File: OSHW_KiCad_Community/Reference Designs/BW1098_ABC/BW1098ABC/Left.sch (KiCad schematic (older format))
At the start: 20 parts, among them J2 BBR43-24KB533 for camera modu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

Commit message: got abc deriv reference started. Pulled in connectors etc
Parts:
- removed C10, C12, C8: 10uF 0603, symbol depthAI_sch:GRM188R61A106ME69D
- removed C11, C7, C9: 0.1uF 0402, symbol depthAI_sch:GRM188R61A106ME69D
- removed FB4, FB5, FB6: 600R/100MHz, symbol depthAI_sch:2508056017Y2
- removed J2: BBR43-24KB533 for camera module TG161B-201, symbol depthAI_sch:TG161B-201_Connector
- removed R10, R4, R5, R6, R7, R8, R9: 0R 0603, symbol depthAI_sch:CRCW06030000Z0EA
- removed R11, R3: 10K 0402, symbol depthAI_sch:RC0402FR-1310KL
- removed R12: 0R 0402, symbol depthAI_sch:CRCW04020000Z0ED
- added C? (x3): 10uF 0603, symbol depthAI_sch:GRM188R61A106ME69D
- added C? (x3): 0.1uF 0402, symbol depthAI_sch:GRM188R61A106ME69D
- added FB? (x3): 600R/100MHz, symbol depthAI_sch:2508056017Y2
- added J?: BBR43-24KB533 for camera module TG161B-201, symbol depthAI_sch:TG161B-201_Connector
- added R? (x7): 0R 0603, symbol depthAI_sch:CRCW06030000Z0EA
- added R? (x2): 10K 0402, symbol depthAI_sch:RC0402FR-1310KL
- added R?: 0R 0402, symbol depthAI_sch:CRCW04020000Z0ED
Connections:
- net labels removed: 10V
- wire segments 87 -> 84

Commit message: skeleton complete, most footprints assigned, still need to check the transferred ones for dims
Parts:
- C? (x3): footprint (none) -> Capacitor_SMD:C_0201_0603Metric
- C? (x3): footprint (none) -> Capacitor_SMD:C_01005_0402Metric
- FB? (x3): footprint (none) -> Ferrite_THT:LairdTech_28C0236-0JW-10
- R? (x10): footprint (none) -> Resistor_SMD:R_0402_1005Metric
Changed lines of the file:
@@
 $Descr A3 16535 11693
 encoding utf-8
-Sheet 5 5
+Sheet 5 6
 Title ""
 Date ""
@@
 F 0 "FB?" H 1400 950 60  0000 L BNN
 F 1 "600R/100MHz" H 1400 770 60  0000 L BNN
-F 2 "" H 1400 770 60  0001 C CNN
+F 2 "Ferrite_THT:LairdTech_28C0236-0JW-10" H 1400 770 60  0001 C CNN
 F 3 "" H 1400 770 60  0000 C CNN
 	1    1300 900
@@
 F 0 "C?" V 6810 5760 60  0000 R TNN
 F 1 "10uF 0603" V 6710 5760 60  0000 R TNN
-F 2 "" H 6710 5760 60  0001 C CNN
+F 2 "Capacitor_SMD:C_0201_0603Metric" H 6710 5760 60  0001 C CNN
 F 3 "" H 6710 5760 60  0000 C CNN
 F 4 "10V" V 700 750 60  0001 C CNN "Voltage Rating"
@@
 F 0 "C?" V 6210 5760 60  0000 R TNN
 F 1 "0.1uF 0402" V 6110 5760 60  0000 R TNN
-F 2 "" H 6110 5760 60  0001 C CNN
+F 2 "Capacitor_SMD:C_01005_0402Metric" H 6110 5760 60  0001 C CNN
 F 3 "" H 6110 5760 60  0000 C CNN
 F 4 "10V" V 700 750 60  0001 C CNN "Voltage Rating"
@@
 F 0 "C?" V 7510 5760 60  0000 R TNN
 F 1 "0.1uF 0402" V 7410 5760 60  0000 R TNN
-F 2 "" H 7410 5760 60  0001 C CNN
+F 2 "Capacitor_SMD:C_01005_0402Metric" H 7410 5760 60  0001 C CNN
 F 3 "" H 7410 5760 60  0000 C CNN
 F 4 "10V" V 700 750 60  0001 C CNN "Voltage Rating"
@@
 F 0 "R?" V 2910 6320 60  0000 R TNN
 F 1 "0R 0603" V 2810 6320 60  0000 R TNN
-F 2 "" H 2810 6320 60  0001 C CNN
+F 2 "Resistor_SMD:R_0402_1005Metric" H 2810 6320 60  0001 C CNN
 F 3 "" H 2810 6320 60  0000 C CNN
 	1    2700 6350
@@
 F 0 "R?" V 3410 6320 60  0000 R TNN
 F 1 "0R 0603" V 3310 6320 60  0000 R TNN
-F 2 "" H 3310 6320 60  0001 C CNN
+F 2 "Resistor_SMD:R_0402_1005Metric" H 3310 6320 60  0001 C CNN
 F 3 "" H 3310 6320 60  0000 C CNN
 	1    3200 6350
@@
 F 0 "R?" V 3910 6320 60  0000 R TNN
 F 1 "0R 0603" V 3810 6320 60  0000 R TNN
-F 2 "" H 3810 6320 60  0001 C CNN
+F 2 "Resistor_SMD:R_0402_1005Metric" H 3810 6320 60  0001 C CNN
 F 3 "" H 3810 6320 60  0000 C CNN
 	1    3700 6350
@@
 F 0 "R?" H 3340 5930 60  0000 L BNN
 F 1 "0R 0603" H 3340 5770 60  0000 L BNN
-F 2 "" H 3340 5770 60  0001 C CNN
+F 2 "Resistor_SMD:R_0402_1005Metric" H 3340 5770 60  0001 C CNN
 F 3 "" H 3340 5770 60  0000 C CNN
 	1    3250 5900
@@
 F 0 "R?" H 2840 5930 60  0000 L BNN
 F 1 "0R 0603" H 2840 5770 60  0000 L BNN
-F 2 "" H 2840 5770 60  0001 C CNN
+F 2 "Resistor_SMD:R_0402_1005Metric" H 2840 5770 60  0001 C CNN
 F 3 "" H 2840 5770 60  0000 C CNN
 	1    2750 5900
@@
 F 0 "R?" H 3340 6430 60  0000 L BNN
 F 1 "0R 0603" H 3340 6270 60  0000 L BNN
-F 2 "" H 3340 6270 60  0001 C CNN
+F 2 "Resistor_SMD:R_0402_1005Metric" H 3340 6270 60  0001 C CNN
 F 3 "" H 3340 6270 60  0000 C CNN
 	1    3250 6400
@@
 F 0 "FB?" H 1400 1250 60  0000 L BNN
 F 1 "600R/100MHz" H 1400 1070 60  0000 L BNN
-F 2 "" H 1400 1070 60  0001 C CNN
+F 2 "Ferrite_THT:LairdTech_28C0236-0JW-10" H 1400 1070 60  0001 C CNN
 F 3 "" H 1400 1070 60  0000 C CNN
 	1    1300 1200
@@
 F 0 "R?" H 2840 6430 60  0000 L BNN
 F 1 "0R 0603" H 2840 6270 60  0000 L BNN
-F 2 "" H 2840 6270 60  0001 C CNN
+F 2 "Resistor_SMD:R_0402_1005Metric" H 2840 6270 60  0001 C CNN
 F 3 "" H 2840 6270 60  0000 C CNN
 	1    2750 6400
@@
 F 0 "FB?" H 1400 1550 60  0000 L BNN
 F 1 "600R/100MHz" H 1400 1370 60  0000 L BNN
-F 2 "" H 1400 1370 60  0001 C CNN
+F 2 "Ferrite_THT:LairdTech_28C0236-0JW-10" H 1400 1370 60  0001 C CNN
 F 3 "" H 1400 1370 60  0000 C CNN
 	1    1300 1500
@@
 F 0 "R?" H 2290 6880 60  0000 L BNN
 F 1 "10K 0402" H 2290 6720 60  0000 L BNN
-F 2 "" H 2290 6720 60  0001 C CNN
+F 2 "Resistor_SMD:R_0402_1005Metric" H 2290 6720 60  0001 C CNN
 F 3 "" H 2290 6720 60  0000 C CNN
 	1    2200 6850
@@
 F 0 "R?" H 9940 3530 60  0000 L BNN
 F 1 "10K 0402" H 9950 3600 60  0000 L BNN
-F 2 "" H 9940 3370 60  0001 C CNN
+F 2 "Resistor_SMD:R_0402_1005Metric" H 9940 3370 60  0001 C CNN
 F 3 "" H 9940 3370 60  0000 C CNN
 	1    9850 3500
@@
 F 0 "R?" H 9940 3930 60  0000 L BNN
 F 1 "0R 0402" H 9940 3770 60  0000 L BNN
-F 2 "" H 9940 3770 60  0001 C CNN
+F 2 "Resistor_SMD:R_0402_1005Metric" H 9940 3770 60  0001 C CNN
 F 3 "" H 9940 3770 60  0000 C CNN
 	1    9850 3900
@@
 F 0 "C?" V 8710 5760 60  0000 R TNN
 F 1 "0.1uF 0402" V 8610 5760 60  0000 R TNN
-F 2 "" H 8610 5760 60  0001 C CNN
+F 2 "Capacitor_SMD:C_01005_0402Metric" H 8610 5760 60  0001 C CNN
 F 3 "" H 8610 5760 60  0000 C CNN
 F 4 "10V" V 700 750 60  0001 C CNN "Voltage Rating"
@@
 F 0 "C?" V 9310 5760 60  0000 R TNN
 F 1 "10uF 0603" V 9210 5760 60  0000 R TNN
-F 2 "" H 9210 5760 60  0001 C CNN
+F 2 "Capacitor_SMD:C_0201_0603Metric" H 9210 5760 60  0001 C CNN
 F 3 "" H 9210 5760 60  0000 C CNN
 F 4 "10V" V 700 750 60  0001 C CNN "Voltage Rating"
@@
 F 0 "C?" V 8100 5750 60  0000 R TNN
 F 1 "10uF 0603" V 8010 5760 60  0000 R TNN
-F 2 "" H 8010 5760 60  0001 C CNN
+F 2 "Capacitor_SMD:C_0201_0603Metric" H 8010 5760 60  0001 C CNN
 F 3 "" H 8010 5760 60  0000 C CNN
 F 4 "10V" V 700 750 60  0001 C CNN "Voltage Rating"

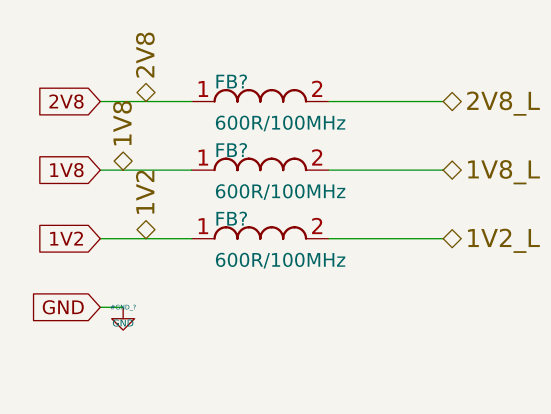
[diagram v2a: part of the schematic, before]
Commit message: schematic edits for BW1098ABC
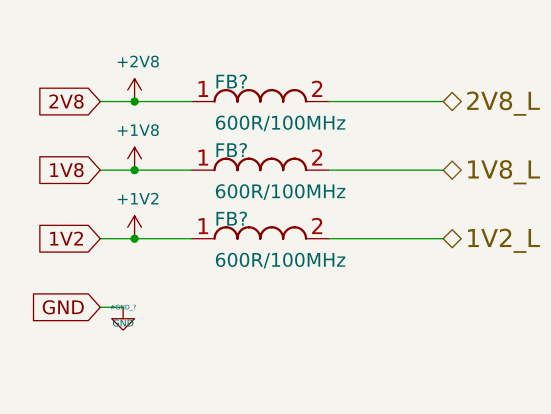
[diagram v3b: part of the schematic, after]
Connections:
- net labels added: +1V2, +1V8, +2V8
- wire segments 84 -> 87
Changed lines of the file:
@@
 $EndBitmap
 Wire Wire Line
-	900  900  1300 900
+	900  900  1050 900
 Wire Wire Line
-	900  1200 1300 1200
-Wire Wire Line
-	900  1500 1300 1500
-Text HLabel 1100 900  1    79   BiDi ~ 0
-2V8
-Text HLabel 1000 1200 1    79   BiDi ~ 0
-1V8
-Text HLabel 1100 1500 1    79   BiDi ~ 0
-1V2
+	900  1500 1050 1500
 Text HLabel 2400 900  2    79   BiDi ~ 0
 2V8_L
@@
 Wire Wire Line
 	8550 3700 10150 3700
+$Comp
+L power:+1V2 #PWR?
+U 1 1 5FFF8485
+P 1050 1500
+AR Path="/604AEAFA/5FFF8485" Ref="#PWR?"  Part="1"
+AR Path="/5FF8D2B3/5FFF8485" Ref="#PWR?"  Part="1"
+F 0 "#PWR?" H 1050 1350 50  0001 C CNN
+F 1 "+1V2" H 1065 1673 50  0000 C CNN
+F 2 "" H 1050 1500 50  0001 C CNN
+F 3 "" H 1050 1500 50  0001 C CNN
+	1    1050 1500
+	1    0    0    -1
+$EndComp
+$Comp
+L power:+1V8 #PWR?
+U 1 1 5FFF848B
+P 1050 1200
+AR Path="/604AEAFA/5FFF848B" Ref="#PWR?"  Part="1"
+AR Path="/5FF8D2B3/5FFF848B" Ref="#PWR?"  Part="1"
+F 0 "#PWR?" H 1050 1050 50  0001 C CNN
+F 1 "+1V8" H 1065 1373 50  0000 C CNN
+F 2 "" H 1050 1200 50  0001 C CNN
+F 3 "" H 1050 1200 50  0001 C CNN
+	1    1050 1200
+	1    0    0    -1
+$EndComp
+$Comp
+L power:+2V8 #PWR?
+U 1 1 5FFF8491
+P 1050 900
+AR Path="/604AEAFA/5FFF8491" Ref="#PWR?"  Part="1"
+AR Path="/5FF8D2B3/5FFF8491" Ref="#PWR?"  Part="1"
+F 0 "#PWR?" H 1050 750 50  0001 C CNN
+F 1 "+2V8" H 1065 1073 50  0000 C CNN
+F 2 "" H 1050 900 50  0001 C CNN
+F 3 "" H 1050 900 50  0001 C CNN
+	1    1050 900
+	1    0    0    -1
+$EndComp
+Connection ~ 1050 900
+Wire Wire Line
+	1050 900  1300 900
+Connection ~ 1050 1200
+Wire Wire Line
+	1050 1200 1300 1200
+Wire Wire Line
+	900  1200 1050 1200
+Connection ~ 1050 1500
+Wire Wire Line
+	1050 1500 1300 1500
 $EndSCHEMATC

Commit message: small stuff
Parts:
- C? (x6): symbol depthAI_sch:GRM188R61A106ME69D -> BW1098ABC-rescue:GRM188R61A106ME69D-depthAI_sch
- FB? (x3): symbol depthAI_sch:2508056017Y2 -> BW1098ABC-rescue:2508056017Y2-depthAI_sch
- J?: symbol depthAI_sch:TG161B-201_Connector -> BW1098ABC-rescue:TG161B-201_Connector-depthAI_sch
- R? (x7): symbol depthAI_sch:CRCW06030000Z0EA -> BW1098ABC-rescue:CRCW06030000Z0EA-depthAI_sch
- R? (x2): symbol depthAI_sch:RC0402FR-1310KL -> BW1098ABC-rescue:RC0402FR-1310KL-depthAI_sch
- R?: symbol depthAI_sch:CRCW04020000Z0ED -> BW1098ABC-rescue:CRCW04020000Z0ED-depthAI_sch
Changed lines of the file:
@@
 Connection ~ 8900 5950
 $Comp
-L depthAI_sch:2508056017Y2 FB?
+L BW1098ABC-rescue:2508056017Y2-depthAI_sch FB?
 U 1 1 603D7B3F
 P 1300 900
@@
 $EndComp
 $Comp
-L depthAI_sch:GRM188R61A106ME69D C?
+L BW1098ABC-rescue:GRM188R61A106ME69D-depthAI_sch C?
 U 1 1 603D7B46
 P 6700 5850
@@
 $EndComp
 $Comp
-L depthAI_sch:GRM188R61A106ME69D C?
+L BW1098ABC-rescue:GRM188R61A106ME69D-depthAI_sch C?
 U 1 1 603D7B4D
 P 6100 5850
@@
 $EndComp
 $Comp
-L depthAI_sch:GRM188R61A106ME69D C?
+L BW1098ABC-rescue:GRM188R61A106ME69D-depthAI_sch C?
 U 1 1 603D7B54
 P 7400 5850
@@
 $EndComp
 $Comp
-L depthAI_sch:TG161B-201_Connector J?
+L BW1098ABC-rescue:TG161B-201_Connector-depthAI_sch J?
 U 1 1 603D7B5A
 P 6750 3300
@@
 $EndComp
 $Comp
-L depthAI_sch:CRCW06030000Z0EA R?
+L BW1098ABC-rescue:CRCW06030000Z0EA-depthAI_sch R?
 U 1 1 603D7B60
 P 2700 6350
@@
 $EndComp
 $Comp
-L depthAI_sch:CRCW06030000Z0EA R?
+L BW1098ABC-rescue:CRCW06030000Z0EA-depthAI_sch R?
 U 1 1 603D7B66
 P 3200 6350
@@
 $EndComp
 $Comp
-L depthAI_sch:CRCW06030000Z0EA R?
+L BW1098ABC-rescue:CRCW06030000Z0EA-depthAI_sch R?
 U 1 1 603D7B6C
 P 3700 6350
@@
 $EndComp
 $Comp
-L depthAI_sch:CRCW06030000Z0EA R?
+L BW1098ABC-rescue:CRCW06030000Z0EA-depthAI_sch R?
 U 1 1 603D7B72
 P 3250 5900
@@
 $EndComp
 $Comp
-L depthAI_sch:CRCW06030000Z0EA R?
+L BW1098ABC-rescue:CRCW06030000Z0EA-depthAI_sch R?
 U 1 1 603D7B78
 P 2750 5900
@@
 $EndComp
 $Comp
-L depthAI_sch:CRCW06030000Z0EA R?
+L BW1098ABC-rescue:CRCW06030000Z0EA-depthAI_sch R?
 U 1 1 603D7B7E
 P 3250 6400
@@
 $EndComp
 $Comp
-L depthAI_sch:2508056017Y2 FB?
+L BW1098ABC-rescue:2508056017Y2-depthAI_sch FB?
 U 1 1 603D7B84
 P 1300 1200
@@
 $EndComp
 $Comp
-L depthAI_sch:CRCW06030000Z0EA R?
+L BW1098ABC-rescue:CRCW06030000Z0EA-depthAI_sch R?
 U 1 1 603D7B8A
 P 2750 6400
@@
 $EndComp
 $Comp
-L depthAI_sch:2508056017Y2 FB?
+L BW1098ABC-rescue:2508056017Y2-depthAI_sch FB?
 U 1 1 603D7B90
 P 1300 1500
@@
 $EndComp
 $Comp
-L depthAI_sch:RC0402FR-1310KL R?
+L BW1098ABC-rescue:RC0402FR-1310KL-depthAI_sch R?
 U 1 1 603D7B96
 P 2200 6850
@@
 $EndComp
 $Comp
-L depthAI_sch:RC0402FR-1310KL R?
+L BW1098ABC-rescue:RC0402FR-1310KL-depthAI_sch R?
 U 1 1 603D7B9C
 P 9850 3500
@@
 $EndComp
 $Comp
-L depthAI_sch:CRCW04020000Z0ED R?
+L BW1098ABC-rescue:CRCW04020000Z0ED-depthAI_sch R?
 U 1 1 603D7BA2
 P 9850 3900
@@
 $EndComp
 $Comp
-L depthAI_sch:GRM188R61A106ME69D C?
+L BW1098ABC-rescue:GRM188R61A106ME69D-depthAI_sch C?
 U 1 1 603D7BA9
 P 8600 5850
@@
 $EndComp
 $Comp
-L depthAI_sch:GRM188R61A106ME69D C?
+L BW1098ABC-rescue:GRM188R61A106ME69D-depthAI_sch C?
 U 1 1 603D7BB0
 P 9200 5850
@@
 $EndComp
 $Comp
-L depthAI_sch:GRM188R61A106ME69D C?
+L BW1098ABC-rescue:GRM188R61A106ME69D-depthAI_sch C?
 U 1 1 603D7BB7
 P 8000 5850

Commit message: all footprints associated on bw1098abc board except two I need to clarify with Brian. Need to talk to chris about power
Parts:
- C? (x3): footprint Capacitor_SMD:C_0201_0603Metric -> Capacitor_SMD:C_0603_1608Metric
- C? (x3): footprint Capacitor_SMD:C_01005_0402Metric -> Capacitor_SMD:C_0402_1005Metric
- FB? (x3): footprint Ferrite_THT:LairdTech_28C0236-0JW-10 -> OSHW_LuxonisMaster_20201223:2508056017Y2
- R? (x7): footprint Resistor_SMD:R_0402_1005Metric -> Resistor_SMD:R_0603_1608Metric
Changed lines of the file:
@@
 F 0 "FB?" H 1400 950 60  0000 L BNN
 F 1 "600R/100MHz" H 1400 770 60  0000 L BNN
-F 2 "Ferrite_THT:LairdTech_28C0236-0JW-10" H 1400 770 60  0001 C CNN
+F 2 "OSHW_LuxonisMaster_20201223:2508056017Y2" H 1400 770 60  0001 C CNN
 F 3 "" H 1400 770 60  0000 C CNN
 	1    1300 900
@@
 F 0 "C?" V 6810 5760 60  0000 R TNN
 F 1 "10uF 0603" V 6710 5760 60  0000 R TNN
-F 2 "Capacitor_SMD:C_0201_0603Metric" H 6710 5760 60  0001 C CNN
+F 2 "Capacitor_SMD:C_0603_1608Metric" H 6710 5760 60  0001 C CNN
 F 3 "" H 6710 5760 60  0000 C CNN
 F 4 "10V" V 700 750 60  0001 C CNN "Voltage Rating"
@@
 F 0 "C?" V 6210 5760 60  0000 R TNN
 F 1 "0.1uF 0402" V 6110 5760 60  0000 R TNN
-F 2 "Capacitor_SMD:C_01005_0402Metric" H 6110 5760 60  0001 C CNN
+F 2 "Capacitor_SMD:C_0402_1005Metric" H 6110 5760 60  0001 C CNN
 F 3 "" H 6110 5760 60  0000 C CNN
 F 4 "10V" V 700 750 60  0001 C CNN "Voltage Rating"
@@
 F 0 "C?" V 7510 5760 60  0000 R TNN
 F 1 "0.1uF 0402" V 7410 5760 60  0000 R TNN
-F 2 "Capacitor_SMD:C_01005_0402Metric" H 7410 5760 60  0001 C CNN
+F 2 "Capacitor_SMD:C_0402_1005Metric" H 7410 5760 60  0001 C CNN
 F 3 "" H 7410 5760 60  0000 C CNN
 F 4 "10V" V 700 750 60  0001 C CNN "Voltage Rating"
@@
 F 0 "R?" V 2910 6320 60  0000 R TNN
 F 1 "0R 0603" V 2810 6320 60  0000 R TNN
-F 2 "Resistor_SMD:R_0402_1005Metric" H 2810 6320 60  0001 C CNN
+F 2 "Resistor_SMD:R_0603_1608Metric" H 2810 6320 60  0001 C CNN
 F 3 "" H 2810 6320 60  0000 C CNN
 	1    2700 6350
@@
 F 0 "R?" V 3410 6320 60  0000 R TNN
 F 1 "0R 0603" V 3310 6320 60  0000 R TNN
-F 2 "Resistor_SMD:R_0402_1005Metric" H 3310 6320 60  0001 C CNN
+F 2 "Resistor_SMD:R_0603_1608Metric" H 3310 6320 60  0001 C CNN
 F 3 "" H 3310 6320 60  0000 C CNN
 	1    3200 6350
@@
 F 0 "R?" V 3910 6320 60  0000 R TNN
 F 1 "0R 0603" V 3810 6320 60  0000 R TNN
-F 2 "Resistor_SMD:R_0402_1005Metric" H 3810 6320 60  0001 C CNN
+F 2 "Resistor_SMD:R_0603_1608Metric" H 3810 6320 60  0001 C CNN
 F 3 "" H 3810 6320 60  0000 C CNN
 	1    3700 6350
@@
 F 0 "R?" H 3340 5930 60  0000 L BNN
 F 1 "0R 0603" H 3340 5770 60  0000 L BNN
-F 2 "Resistor_SMD:R_0402_1005Metric" H 3340 5770 60  0001 C CNN
+F 2 "Resistor_SMD:R_0603_1608Metric" H 3340 5770 60  0001 C CNN
 F 3 "" H 3340 5770 60  0000 C CNN
 	1    3250 5900
@@
 F 0 "R?" H 2840 5930 60  0000 L BNN
 F 1 "0R 0603" H 2840 5770 60  0000 L BNN
-F 2 "Resistor_SMD:R_0402_1005Metric" H 2840 5770 60  0001 C CNN
+F 2 "Resistor_SMD:R_0603_1608Metric" H 2840 5770 60  0001 C CNN
 F 3 "" H 2840 5770 60  0000 C CNN
 	1    2750 5900
@@
 F 0 "R?" H 3340 6430 60  0000 L BNN
 F 1 "0R 0603" H 3340 6270 60  0000 L BNN
-F 2 "Resistor_SMD:R_0402_1005Metric" H 3340 6270 60  0001 C CNN
+F 2 "Resistor_SMD:R_0603_1608Metric" H 3340 6270 60  0001 C CNN
 F 3 "" H 3340 6270 60  0000 C CNN
 	1    3250 6400
@@
 F 0 "FB?" H 1400 1250 60  0000 L BNN
 F 1 "600R/100MHz" H 1400 1070 60  0000 L BNN
-F 2 "Ferrite_THT:LairdTech_28C0236-0JW-10" H 1400 1070 60  0001 C CNN
+F 2 "OSHW_LuxonisMaster_20201223:2508056017Y2" H 1400 1070 60  0001 C CNN
 F 3 "" H 1400 1070 60  0000 C CNN
 	1    1300 1200
@@
 F 0 "R?" H 2840 6430 60  0000 L BNN
 F 1 "0R 0603" H 2840 6270 60  0000 L BNN
-F 2 "Resistor_SMD:R_0402_1005Metric" H 2840 6270 60  0001 C CNN
+F 2 "Resistor_SMD:R_0603_1608Metric" H 2840 6270 60  0001 C CNN
 F 3 "" H 2840 6270 60  0000 C CNN
 	1    2750 6400
@@
 F 0 "FB?" H 1400 1550 60  0000 L BNN
 F 1 "600R/100MHz" H 1400 1370 60  0000 L BNN
-F 2 "Ferrite_THT:LairdTech_28C0236-0JW-10" H 1400 1370 60  0001 C CNN
+F 2 "OSHW_LuxonisMaster_20201223:2508056017Y2" H 1400 1370 60  0001 C CNN
 F 3 "" H 1400 1370 60  0000 C CNN
 	1    1300 1500
@@
 F 0 "C?" V 8710 5760 60  0000 R TNN
 F 1 "0.1uF 0402" V 8610 5760 60  0000 R TNN
-F 2 "Capacitor_SMD:C_01005_0402Metric" H 8610 5760 60  0001 C CNN
+F 2 "Capacitor_SMD:C_0402_1005Metric" H 8610 5760 60  0001 C CNN
 F 3 "" H 8610 5760 60  0000 C CNN
 F 4 "10V" V 700 750 60  0001 C CNN "Voltage Rating"
@@
 F 0 "C?" V 9310 5760 60  0000 R TNN
 F 1 "10uF 0603" V 9210 5760 60  0000 R TNN
-F 2 "Capacitor_SMD:C_0201_0603Metric" H 9210 5760 60  0001 C CNN
+F 2 "Capacitor_SMD:C_0603_1608Metric" H 9210 5760 60  0001 C CNN
 F 3 "" H 9210 5760 60  0000 C CNN
 F 4 "10V" V 700 750 60  0001 C CNN "Voltage Rating"
@@
 F 0 "C?" V 8100 5750 60  0000 R TNN
 F 1 "10uF 0603" V 8010 5760 60  0000 R TNN
-F 2 "Capacitor_SMD:C_0201_0603Metric" H 8010 5760 60  0001 C CNN
+F 2 "Capacitor_SMD:C_0603_1608Metric" H 8010 5760 60  0001 C CNN
 F 3 "" H 8010 5760 60  0000 C CNN
 F 4 "10V" V 700 750 60  0001 C CNN "Voltage Rating"

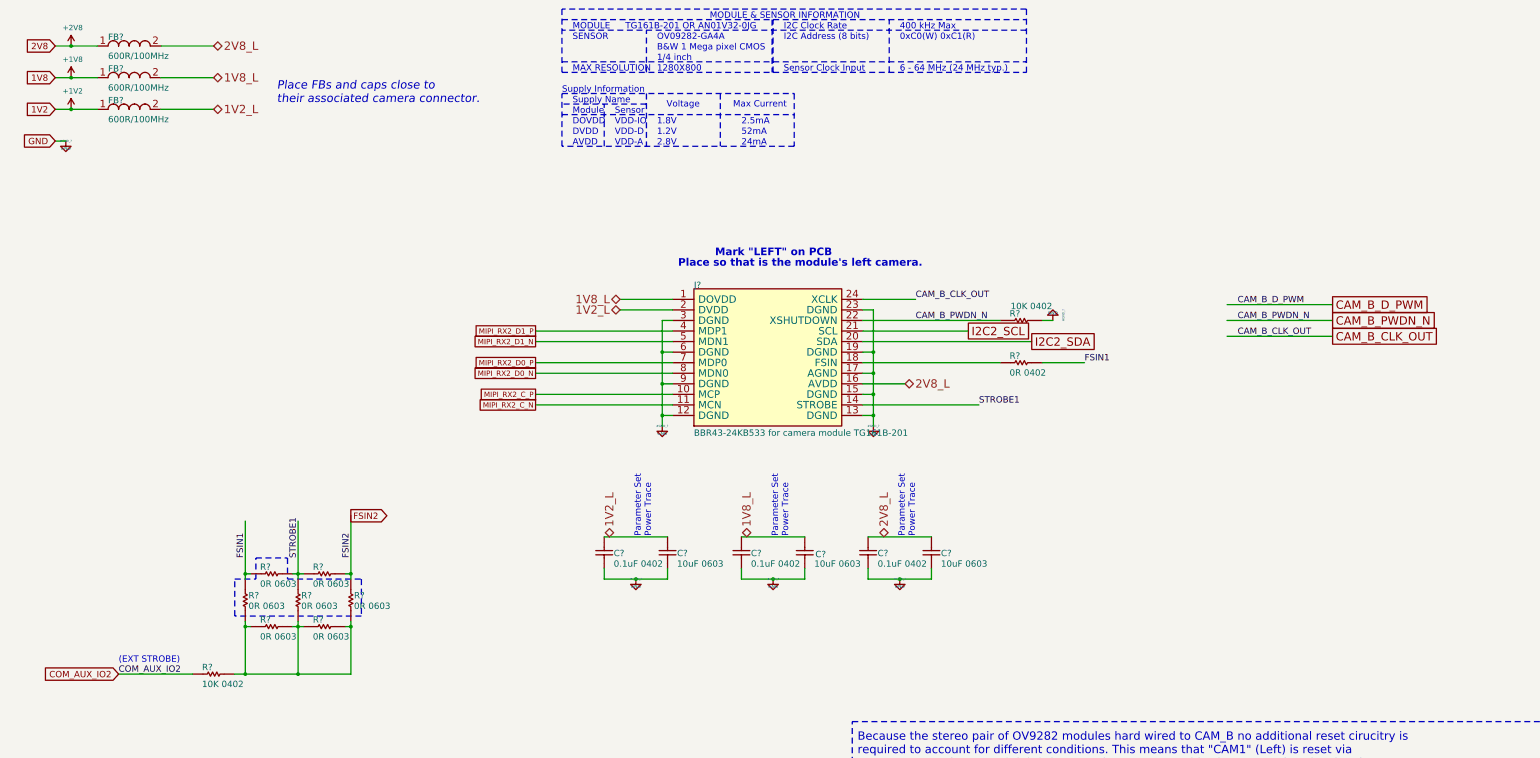
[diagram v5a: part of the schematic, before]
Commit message: added busses, fixed hierarchical labeling, just need to fix an erc thing with my buses then itll pass
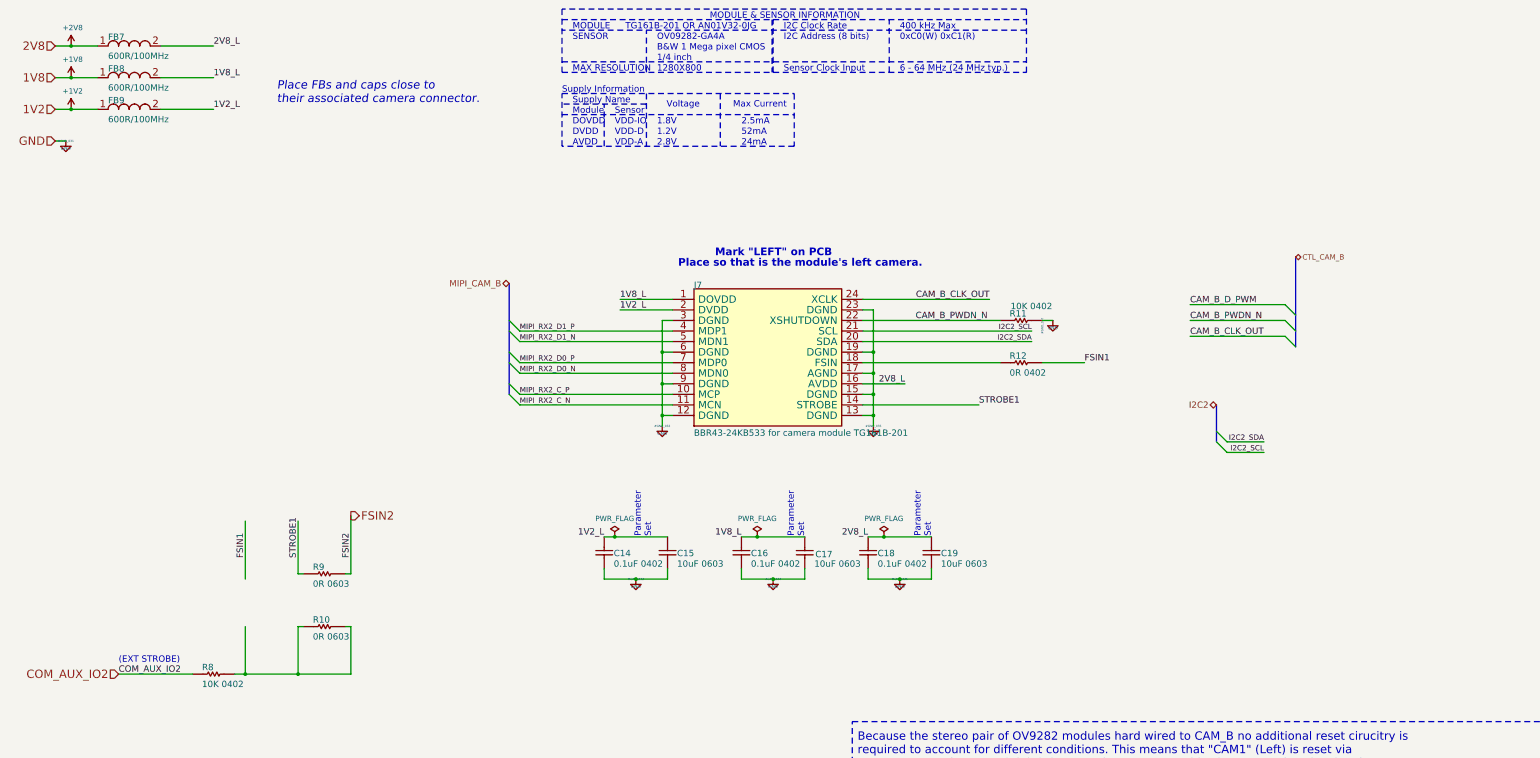
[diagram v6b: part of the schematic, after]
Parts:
- removed R? (x5): 0R 0603, Resistor_SMD:R_0603_1608Metric, symbol BW1098ABC-rescue:CRCW06030000Z0EA-depthAI_sch
- gave numbers to parts that had none: 15
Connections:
- net labels added: CTL_CAM_B, I2C2, MIPI_CAM_B
- wire segments 87 -> 82
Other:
- note added: "Parameter \nSet\n"
- note removed: "Parameter Set\nPower Trace"
